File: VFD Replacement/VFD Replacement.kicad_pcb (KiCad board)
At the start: 0 parts

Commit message: Create Display PCB
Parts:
- added D1: LED, LED_SMD:LED_0402_1005Metric, F.Cu at (133.9, 53.1)
- added D10: LED, LED_SMD:LED_0402_1005Metric, F.Cu at (137.2, 57.0)
- added D11: LED, LED_SMD:LED_0402_1005Metric, F.Cu at (138.0, 53.1)
- added D12: LED, LED_SMD:LED_0402_1005Metric, F.Cu at (138.0, 55.7)
- added D13: LED, LED_SMD:LED_0402_1005Metric, F.Cu at (138.0, 58.3)
- added D14: LED, LED_SMD:LED_0402_1005Metric, F.Cu at (138.8, 54.4)
- added D15: LED, LED_SMD:LED_0402_1005Metric, F.Cu at (138.8, 57.0)
- added D16: LED, LED_SMD:LED_0402_1005Metric, F.Cu at (140.0, 58.3)
- added D17: LED, LED_SMD:LED_0402_1005Metric, F.Cu at (141.3, 54.4)
- added D18: LED, LED_SMD:LED_0402_1005Metric, F.Cu at (141.3, 57.0)
- added D19: LED, LED_SMD:LED_0402_1005Metric, F.Cu at (142.2, 53.1)
- added D2: LED, LED_SMD:LED_0402_1005Metric, F.Cu at (133.1, 54.4)
- added D20: LED, LED_SMD:LED_0402_1005Metric, F.Cu at (142.2, 55.7)
- added D21: LED, LED_SMD:LED_0402_1005Metric, F.Cu at (142.2, 58.3)
- added D22: LED, LED_SMD:LED_0402_1005Metric, F.Cu at (143.0, 54.4)
- added D23: LED, LED_SMD:LED_0402_1005Metric, F.Cu at (143.0, 57.0)
- added D24: LED, LED_SMD:LED_0402_1005Metric, F.Cu at (144.2, 58.3)
- added D25: LED, LED_SMD:LED_0402_1005Metric, F.Cu at (145.5, 54.4)
- added D26: LED, LED_SMD:LED_0402_1005Metric, F.Cu at (145.5, 57.0)
- added D27: LED, LED_SMD:LED_0402_1005Metric, F.Cu at (146.3, 53.1)
- added D28: LED, LED_SMD:LED_0402_1005Metric, F.Cu at (146.3, 55.7)
- added D29: LED, LED_SMD:LED_0402_1005Metric, F.Cu at (146.3, 58.3)
- added D3: LED, LED_SMD:LED_0402_1005Metric, F.Cu at (133.1, 57.0)
- added D30: LED, LED_SMD:LED_0402_1005Metric, F.Cu at (147.2, 54.4)
- added D31: LED, LED_SMD:LED_0402_1005Metric, F.Cu at (147.2, 57.0)
- added D32: LED, LED_SMD:LED_0402_1005Metric, F.Cu at (148.3, 58.3)
- added D33: LED, LED_SMD:LED_0402_1005Metric, F.Cu at (149.7, 54.4)
- added D34: LED, LED_SMD:LED_0402_1005Metric, F.Cu at (149.7, 57.0)
- added D35: LED, LED_SMD:LED_0402_1005Metric, F.Cu at (150.5, 53.1)
- added D36: LED, LED_SMD:LED_0402_1005Metric, F.Cu at (150.5, 55.7)
- added D37: LED, LED_SMD:LED_0402_1005Metric, F.Cu at (150.5, 58.3)
- added D38: LED, LED_SMD:LED_0402_1005Metric, F.Cu at (151.3, 54.4)
- added D39: LED, LED_SMD:LED_0402_1005Metric, F.Cu at (151.3, 57.0)
- added D4: LED, LED_SMD:LED_0402_1005Metric, F.Cu at (133.9, 58.3)
- added D40: LED, LED_SMD:LED_0402_1005Metric, F.Cu at (152.5, 58.3)
- added D41: LED, LED_SMD:LED_0402_1005Metric, F.Cu at (153.8, 54.4)
- added D42: LED, LED_SMD:LED_0402_1005Metric, F.Cu at (153.8, 57.0)
- added D43: LED, LED_SMD:LED_0402_1005Metric, F.Cu at (154.6, 53.1)
- added D44: LED, LED_SMD:LED_0402_1005Metric, F.Cu at (154.6, 55.7)
- added D45: LED, LED_SMD:LED_0402_1005Metric, F.Cu at (154.6, 58.3)
- added D46: LED, LED_SMD:LED_0402_1005Metric, F.Cu at (155.4, 54.4)
- added D47: LED, LED_SMD:LED_0402_1005Metric, F.Cu at (155.4, 57.0)
- added D48: LED, LED_SMD:LED_0402_1005Metric, F.Cu at (156.6, 58.3)
- added D49: LED, LED_SMD:LED_0402_1005Metric, F.Cu at (157.9, 54.4)
- added D5: LED, LED_SMD:LED_0402_1005Metric, F.Cu at (133.9, 55.7)
- added D50: LED, LED_SMD:LED_0402_1005Metric, F.Cu at (157.9, 57.0)
- added D51: LED, LED_SMD:LED_0402_1005Metric, F.Cu at (158.8, 53.1)
- added D52: LED, LED_SMD:LED_0402_1005Metric, F.Cu at (158.8, 55.7)
- added D53: LED, LED_SMD:LED_0402_1005Metric, F.Cu at (158.8, 58.3)
- added D54: LED, LED_SMD:LED_0402_1005Metric, F.Cu at (159.6, 54.4)
- added D55: LED, LED_SMD:LED_0402_1005Metric, F.Cu at (159.6, 57.0)
- added D56: LED, LED_SMD:LED_0402_1005Metric, F.Cu at (160.8, 58.3)
- added D57: LED, LED_SMD:LED_0402_1005Metric, F.Cu at (162.1, 54.4)
- added D58: LED, LED_SMD:LED_0402_1005Metric, F.Cu at (162.1, 57.0)
- added D59: LED, LED_SMD:LED_0402_1005Metric, F.Cu at (162.9, 53.1)
- added D6: LED, LED_SMD:LED_0402_1005Metric, F.Cu at (134.7, 54.4)
- added D60: LED, LED_SMD:LED_0402_1005Metric, F.Cu at (162.9, 55.7)
- added D61: LED, LED_SMD:LED_0402_1005Metric, F.Cu at (162.9, 58.3)
- added D62: LED, LED_SMD:LED_0402_1005Metric, F.Cu at (163.8, 54.4)
- added D63: LED, LED_SMD:LED_0402_1005Metric, F.Cu at (163.8, 57.0)
- added D64: LED, LED_SMD:LED_0402_1005Metric, F.Cu at (164.9, 58.3)
- added D65: LED, LED_SMD:LED_0402_1005Metric, F.Cu at (166.2, 54.4)
- added D66: LED, LED_SMD:LED_0402_1005Metric, F.Cu at (166.2, 57.0)
- added D67: LED, LED_SMD:LED_0402_1005Metric, F.Cu at (167.1, 53.1)
- added D68: LED, LED_SMD:LED_0402_1005Metric, F.Cu at (167.1, 55.7)
- added D69: LED, LED_SMD:LED_0402_1005Metric, F.Cu at (167.1, 58.3)
- added D7: LED, LED_SMD:LED_0402_1005Metric, F.Cu at (134.7, 57.0)
- added D70: LED, LED_SMD:LED_0402_1005Metric, F.Cu at (167.9, 54.4)
- added D71: LED, LED_SMD:LED_0402_1005Metric, F.Cu at (167.9, 57.0)
- added D72: LED, LED_SMD:LED_0402_1005Metric, F.Cu at (169.1, 58.3)
- added D73: LED, LED_SMD:LED_0402_1005Metric, F.Cu at (170.4, 54.4)
- added D74: LED, LED_SMD:LED_0402_1005Metric, F.Cu at (170.4, 57.0)
- added D75: LED, LED_SMD:LED_0402_1005Metric, F.Cu at (171.2, 53.1)
- added D76: LED, LED_SMD:LED_0402_1005Metric, F.Cu at (171.2, 55.7)
- added D77: LED, LED_SMD:LED_0402_1005Metric, F.Cu at (171.2, 58.3)
- added D78: LED, LED_SMD:LED_0402_1005Metric, F.Cu at (172.1, 54.4)
- added D79: LED, LED_SMD:LED_0402_1005Metric, F.Cu at (172.1, 57.0)
- added D8: LED, LED_SMD:LED_0402_1005Metric, F.Cu at (135.9, 58.3)
- added D80: LED, LED_SMD:LED_0402_1005Metric, F.Cu at (173.2, 58.3)
- added D81: LED, LED_SMD:LED_0402_1005Metric, F.Cu at (174.6, 54.4)
- added D82: LED, LED_SMD:LED_0402_1005Metric, F.Cu at (174.6, 57.0)
- added D83: LED, LED_SMD:LED_0402_1005Metric, F.Cu at (175.4, 53.1)
- added D84: LED, LED_SMD:LED_0402_1005Metric, F.Cu at (175.4, 55.7)
- added D85: LED, LED_SMD:LED_0402_1005Metric, F.Cu at (175.4, 58.3)
- added D86: LED, LED_SMD:LED_0402_1005Metric, F.Cu at (176.2, 54.4)
- added D87: LED, LED_SMD:LED_0402_1005Metric, F.Cu at (176.2, 57.0)
- added D88: LED, LED_SMD:LED_0402_1005Metric, F.Cu at (177.4, 58.3)
- added D89: LED, LED_SMD:LED_0402_1005Metric, F.Cu at (178.7, 54.4)
- added D9: LED, LED_SMD:LED_0402_1005Metric, F.Cu at (137.2, 54.4)
- added D90: LED, LED_SMD:LED_0402_1005Metric, F.Cu at (178.7, 57.0)
- added D91: LED, LED_SMD:LED_0402_1005Metric, F.Cu at (179.5, 53.1)
- added D92: LED, LED_SMD:LED_0402_1005Metric, F.Cu at (179.5, 55.7)
- added D93: LED, LED_SMD:LED_0402_1005Metric, F.Cu at (179.5, 58.3)
- added D94: LED, LED_SMD:LED_0402_1005Metric, F.Cu at (180.3, 54.4)
- added D95: LED, LED_SMD:LED_0402_1005Metric, F.Cu at (180.3, 57.0)
- added D96: LED, LED_SMD:LED_0402_1005Metric, F.Cu at (181.5, 58.3)
- added J1: Conn_01x05_Pin, footprints:Conn_1x05 2.5mm, F.Cu at (132.0, 44.2)
- added J2: Conn_01x05_Pin, footprints:Conn_1x05 2.5mm, F.Cu at (172.0, 44.2)
- added J3: Conn_01x06_Pin, footprints:Conn_1x06 2.5mm, F.Cu at (132.0, 69.2)
- added J4: Conn_01x06_Pin, footprints:Conn_1x06 2.5mm, F.Cu at (169.5, 69.2)
- added J5: Conn_01x02_Pin, Connector_PinHeader_2.54mm:PinHeader_1x02_P2.54mm_Vertical, F.Cu at (156.5, 68.6)
- added Q1: MMDT2222A, Package_TO_SOT_SMD:SOT-363_SC-70-6, F.Cu at (131.8, 65.0)
- added Q10: MMDT2222A, Package_TO_SOT_SMD:SOT-363_SC-70-6, F.Cu at (147.4, 48.5)
- added Q2: MMDT2222A, Package_TO_SOT_SMD:SOT-363_SC-70-6, F.Cu at (142.2, 65.0)
- added Q3: MMDT2222A, Package_TO_SOT_SMD:SOT-363_SC-70-6, F.Cu at (169.8, 64.8)
- added Q4: MMDT2222A, Package_TO_SOT_SMD:SOT-363_SC-70-6, F.Cu at (181.4, 64.8)
- added Q5: MMDT2222A, Package_TO_SOT_SMD:SOT-363_SC-70-6, F.Cu at (137.1, 65.0)
- added Q6: MMDT2222A, Package_TO_SOT_SMD:SOT-363_SC-70-6, F.Cu at (175.8, 64.8)
- added Q7: MMDT2222A, Package_TO_SOT_SMD:SOT-363_SC-70-6, F.Cu at (167.7, 47.1)
- added Q8: MMDT2222A, Package_TO_SOT_SMD:SOT-363_SC-70-6, F.Cu at (182.7, 47.1)
- added Q9: MMDT2222A, Package_TO_SOT_SMD:SOT-363_SC-70-6, F.Cu at (130.7, 48.4)
- added R1: 10k, Resistor_SMD:R_0603_1608Metric_Pad0.98x0.95mm_HandSolder, F.Cu at (172.0, 46.9)
- added R10: 10k, Resistor_SMD:R_0603_1608Metric_Pad0.98x0.95mm_HandSolder, F.Cu at (174.6, 50.3)
- added R11: 10k, Resistor_SMD:R_0603_1608Metric_Pad0.98x0.95mm_HandSolder, F.Cu at (177.0, 50.3)
- added R12: 10k, Resistor_SMD:R_0603_1608Metric_Pad0.98x0.95mm_HandSolder, F.Cu at (179.4, 50.2)
- added R13: 10k, Resistor_SMD:R_0603_1608Metric_Pad0.98x0.95mm_HandSolder, F.Cu at (134.6, 50.2)
- added R14: 10k, Resistor_SMD:R_0603_1608Metric_Pad0.98x0.95mm_HandSolder, F.Cu at (137.0, 50.2)
- added R15: 10k, Resistor_SMD:R_0603_1608Metric_Pad0.98x0.95mm_HandSolder, F.Cu at (142.0, 50.3)
- added R16: 10k, Resistor_SMD:R_0603_1608Metric_Pad0.98x0.95mm_HandSolder, F.Cu at (139.6, 50.2)
- added R17: 1k, Resistor_SMD:R_0603_1608Metric_Pad0.98x0.95mm_HandSolder, F.Cu at (160.2, 47.4)
- added R18: 1k, Resistor_SMD:R_0603_1608Metric_Pad0.98x0.95mm_HandSolder, F.Cu at (41.1, 39.9)
- added R19: 1k, Resistor_SMD:R_0603_1608Metric_Pad0.98x0.95mm_HandSolder, F.Cu at (45.8, 25.1)
- added R2: 10k, Resistor_SMD:R_0603_1608Metric_Pad0.98x0.95mm_HandSolder, F.Cu at (174.6, 46.9)
- added R20: 1k, Resistor_SMD:R_0603_1608Metric_Pad0.98x0.95mm_HandSolder, F.Cu at (45.8, 28.1)
- added R21: 1k, Resistor_SMD:R_0603_1608Metric_Pad0.98x0.95mm_HandSolder, F.Cu at (45.8, 31.0)
- added R22: 1k, Resistor_SMD:R_0603_1608Metric_Pad0.98x0.95mm_HandSolder, F.Cu at (45.8, 34.0)
- added R23: 1k, Resistor_SMD:R_0603_1608Metric_Pad0.98x0.95mm_HandSolder, F.Cu at (144.9, 48.7)
- added R24: 1k, Resistor_SMD:R_0603_1608Metric_Pad0.98x0.95mm_HandSolder, F.Cu at (149.9, 48.7)
- added R25: 10k, Resistor_SMD:R_0603_1608Metric_Pad0.98x0.95mm_HandSolder, F.Cu at (129.9, 44.9)
- added R3: 10k, Resistor_SMD:R_0603_1608Metric_Pad0.98x0.95mm_HandSolder, F.Cu at (177.0, 46.9)
- added R4: 10k, Resistor_SMD:R_0603_1608Metric_Pad0.98x0.95mm_HandSolder, F.Cu at (179.4, 46.9)
- added R5: 10k, Resistor_SMD:R_0603_1608Metric_Pad0.98x0.95mm_HandSolder, F.Cu at (134.6, 46.9)
- added R6: 10k, Resistor_SMD:R_0603_1608Metric_Pad0.98x0.95mm_HandSolder, F.Cu at (137.0, 46.9)
- added R7: 10k, Resistor_SMD:R_0603_1608Metric_Pad0.98x0.95mm_HandSolder, F.Cu at (142.0, 46.9)
- added R8: 10k, Resistor_SMD:R_0603_1608Metric_Pad0.98x0.95mm_HandSolder, F.Cu at (139.6, 46.9)
- added R9: 10k, Resistor_SMD:R_0603_1608Metric_Pad0.98x0.95mm_HandSolder, F.Cu at (172.0, 50.3)
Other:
- board outline added: 65 x 27.5 mm
- copper layers 0 -> 2
- board text added: "-27V"
- board text added: "-5V"

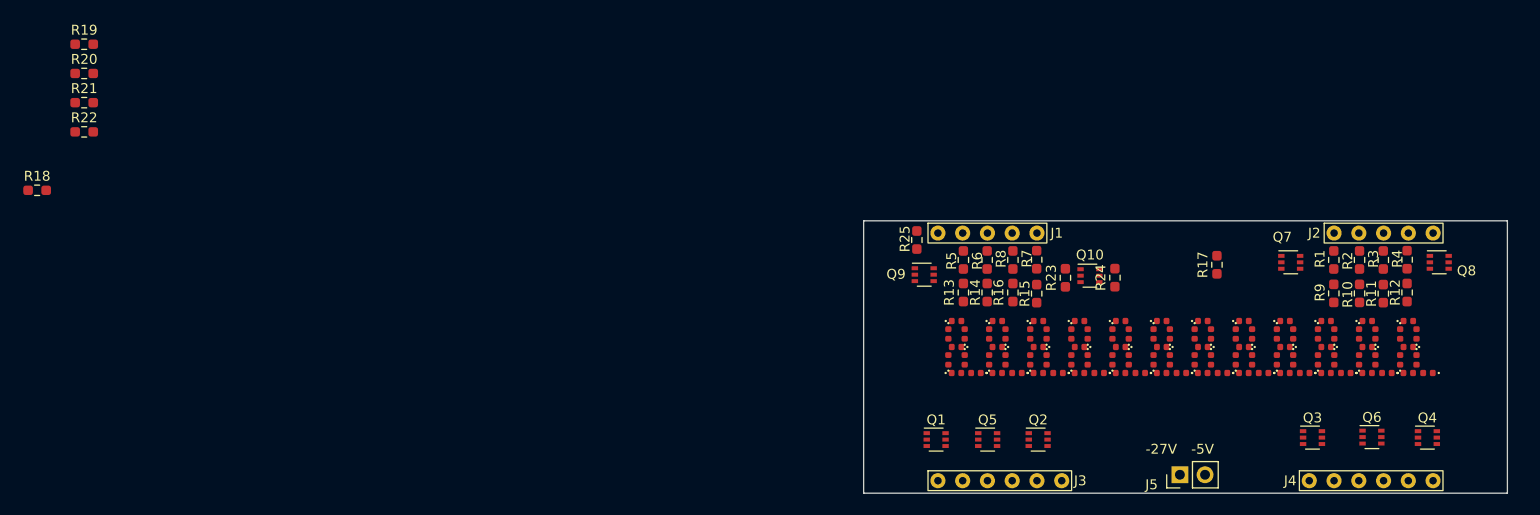
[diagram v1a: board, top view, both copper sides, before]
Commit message: Update VFD Replacement layout
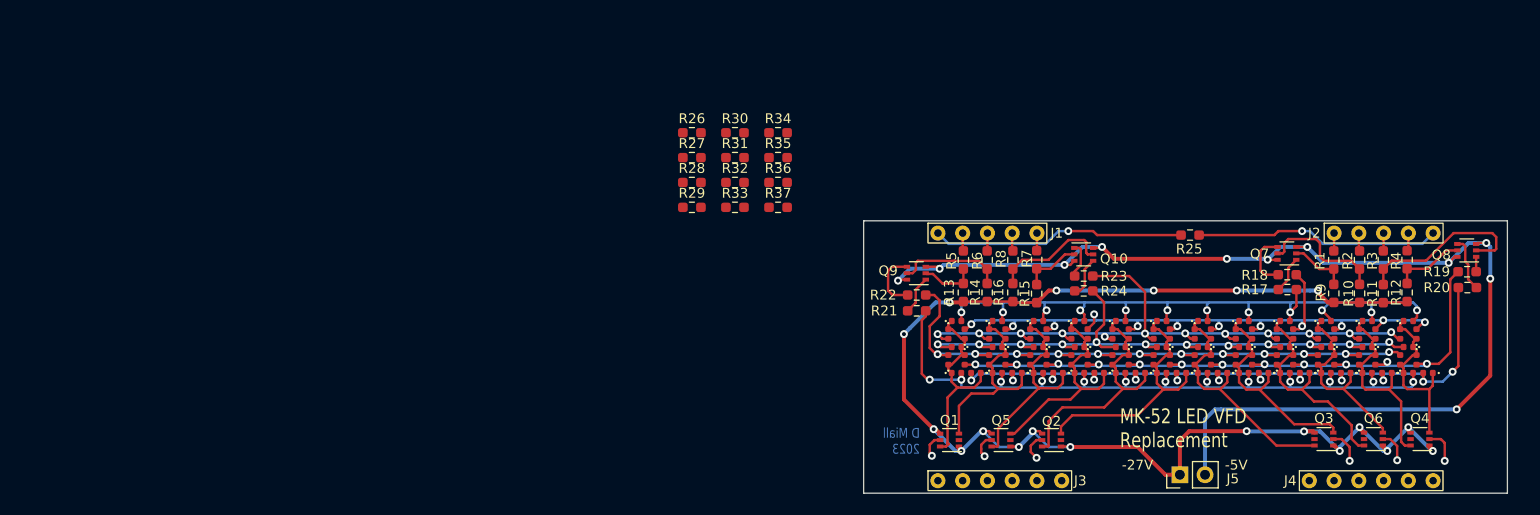
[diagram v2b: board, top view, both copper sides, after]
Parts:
- added R26: 12k, Resistor_SMD:R_0603_1608Metric_Pad0.98x0.95mm_HandSolder, F.Cu at (107.2, 34.1)
- added R27: 12k, Resistor_SMD:R_0603_1608Metric_Pad0.98x0.95mm_HandSolder, F.Cu at (107.2, 36.6)
- added R28: 12k, Resistor_SMD:R_0603_1608Metric_Pad0.98x0.95mm_HandSolder, F.Cu at (107.2, 39.1)
- added R29: 12k, Resistor_SMD:R_0603_1608Metric_Pad0.98x0.95mm_HandSolder, F.Cu at (107.2, 41.6)
- added R30: 12k, Resistor_SMD:R_0603_1608Metric_Pad0.98x0.95mm_HandSolder, F.Cu at (111.5, 34.1)
- added R31: 12k, Resistor_SMD:R_0603_1608Metric_Pad0.98x0.95mm_HandSolder, F.Cu at (111.5, 36.6)
- added R32: 12k, Resistor_SMD:R_0603_1608Metric_Pad0.98x0.95mm_HandSolder, F.Cu at (111.5, 39.1)
- added R33: 12k, Resistor_SMD:R_0603_1608Metric_Pad0.98x0.95mm_HandSolder, F.Cu at (111.5, 41.6)
- added R34: 12k, Resistor_SMD:R_0603_1608Metric_Pad0.98x0.95mm_HandSolder, F.Cu at (115.9, 34.1)
- added R35: 12k, Resistor_SMD:R_0603_1608Metric_Pad0.98x0.95mm_HandSolder, F.Cu at (115.9, 36.6)
- added R36: 12k, Resistor_SMD:R_0603_1608Metric_Pad0.98x0.95mm_HandSolder, F.Cu at (115.9, 39.1)
- added R37: 12k, Resistor_SMD:R_0603_1608Metric_Pad0.98x0.95mm_HandSolder, F.Cu at (115.9, 41.6)
- R1, R2, R3, R4, R5, R6, R7, R8: value 10k -> 1k
- R10, R11, R12, R13, R14, R15, R16, R9: value 10k -> 12k
- R17, R18, R19, R20, R21, R22, R23, R24: value 1k -> 2k4
- moved R19 141.5 mm to (185.5, 48.1)
- moved R20 141.3 mm to (185.5, 49.7)
- moved R18 126.5 mm to (167.3, 48.4), turned to 180 degrees
- moved R21 86.6 mm to (129.9, 52.0), turned to 180 degrees
- moved R22 85.7 mm to (129.9, 50.5), turned to 180 degrees
- moved R25 27.6 mm to (157.5, 44.4), turned to 180 degrees
- moved R17 7.54 mm to (167.3, 49.9), turned to 180 degrees
- moved R24 3.42 mm to (146.8, 50.0), turned to 180 degrees
- moved Q8 3.02 mm to (185.4, 46.0), turned to 180 degrees
- moved Q10 2.24 mm to (146.8, 46.4)
- moved R23 1.86 mm to (146.8, 48.5), turned to 180 degrees
- moved Q1 1.35 mm to (133.2, 65.1), turned to 180 degrees
- moved Q2 1.35 mm to (143.5, 65.1), turned to 180 degrees
- moved Q5 1.35 mm to (138.4, 65.1), turned to 180 degrees
- moved Q3 1.16 mm to (171.0, 65.0), turned to 180 degrees
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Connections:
- Q1 pad 2: /G1 -> Net-(Q1A-B1)
- Q1 pad 5: /G2 -> Net-(Q1B-B2)
- Q2 pad 2: /G5 -> Net-(Q2A-B1)
- Q2 pad 5: /G6 -> Net-(Q2B-B2)
- Q3 pad 2: /G7 -> Net-(Q3A-B1)
- Q3 pad 5: /G8 -> Net-(Q3B-B2)
- Q4 pad 2: /G11 -> Net-(Q4A-B1)
- Q4 pad 3: /G12s -> unconnected-(Q4B-C2-Pad3)
- Q4 pad 5: /G12 -> Net-(Q4B-B2)
- Q4 pad 6: /G11s -> unconnected-(Q4A-C1-Pad6)
- Q5 pad 2: /G3 -> Net-(Q5A-B1)
- Q5 pad 5: /G4 -> Net-(Q5B-B2)
- Q6 pad 2: /G9 -> Net-(Q6A-B1)
- Q6 pad 5: /G10 -> Net-(Q6B-B2)
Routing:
- net -27V: track 0.00 -> 138.7 mm, vias 0 -> 19
- net +22V: track 0.00 -> 122.0 mm, vias 0 -> 11
- net /DPs: track 0.00 -> 74.4 mm, vias 0 -> 13
- net /Ds: track 0.00 -> 74.3 mm, vias 0 -> 13
- net /As: track 0.00 -> 72.8 mm, vias 0 -> 12
- net /Cs: track 0.00 -> 71.7 mm, vias 0 -> 12
- net /Es: track 0.00 -> 70.0 mm, vias 0 -> 12
- net /Bs: track 0.00 -> 69.8 mm, vias 0 -> 12
- net /Fs: track 0.00 -> 69.7 mm, vias 0 -> 12
- net /Gs: track 0.00 -> 69.1 mm, vias 0 -> 12
- net /G6s: track 0.00 -> 26.0 mm
- net /Fil A: track 0.00 -> 25.7 mm, vias 0 -> 1
- net /G7s: track 0.00 -> 25.3 mm
- net /G5s: track 0.00 -> 25.2 mm
- net /Fil B: track 0.00 -> 24.8 mm, vias 0 -> 1
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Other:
- board text added: "D Miall 2023"
- board text added: "JLCJLCJLCJLC"
- board text added: "MK-52 LED VFD Replacement"

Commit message: Complete
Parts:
- removed D1, D10, D11, D12, D13, D14, D15, D16, D17, D18, D19, D2, D20, D21, D22, D23, D24, D25, D26, D27, D28, D29, D3, D30, D31, D32, D33, D34, D35, D36, D37, D38, D39, D4, D40, D41, D42, D43, D44, D45, D46, D47, D48, D49, D5, D50, D51, D52, D53, D54, D55, D56, D57, D58, D59, D6, D60, D61, D62, D63, D64, D65, D66, D67, D68, D69, D7, D70, D71, D72, D73, D74, D75, D76, D77, D78, D79, D8, D80, D81, D82, D83, D84, D85, D86, D87, D88, D89, D9, D90, D91, D92, D93, D94, D95, D96: LED, LED_SMD:LED_0402_1005Metric
- added U1: ~, footprints:display, F.Cu at (148.6, 51.3)
- moved R37 73.4 mm to (184.6, 67.4)
- moved R35 72.2 mm to (181.2, 67.4)
- moved R33 71.2 mm to (177.9, 67.4)
- moved R31 70.2 mm to (174.6, 67.4)
- moved R29 69.1 mm to (171.3, 67.4)
- moved R27 68.2 mm to (168.0, 67.4)
- moved R34 42.7 mm to (142.6, 67.4), turned to 180 degrees
- moved R30 41.3 mm to (135.9, 67.4), turned to 180 degrees
- moved R36 41.3 mm to (145.9, 67.4), turned to 180 degrees
- moved R26 39.9 mm to (129.2, 67.4), turned to 180 degrees
- moved R32 39.6 mm to (139.2, 67.4), turned to 180 degrees
- moved R28 38.0 mm to (132.5, 67.4), turned to 180 degrees
- moved Q3 4.80 mm to (175.7, 63.8), turned to 0 degrees
- moved Q4 4.80 mm to (185.3, 63.8), turned to 0 degrees
- moved Q6 4.80 mm to (180.7, 63.8), turned to 0 degrees
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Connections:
- Q4 pad 3: unconnected-(Q4B-C2-Pad3) -> /G12s
- Q4 pad 6: unconnected-(Q4A-C1-Pad6) -> /G11s
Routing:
- net /Bs: track 69.8 -> 3.66 mm, vias 12 -> 0
- net /As: track 72.8 -> 6.87 mm, vias 12 -> 0
- net /Gs: track 69.1 -> 6.81 mm, vias 12 -> 0
- net /Fs: track 69.7 -> 9.97 mm, vias 12 -> 0
- net /Ds: track 74.3 -> 19.1 mm, vias 13 -> 0
- net /DPs: track 74.4 -> 19.3 mm, vias 13 -> 0
- net /Cs: track 71.7 -> 23.3 mm, vias 12 -> 0
- net /Es: track 70.0 -> 24.5 mm, vias 12 -> 1
- net +22V: track 122.0 -> 103.8 mm, vias 11 -> 8
- net /G5s: track 25.2 -> 14.7 mm
- net -27V: track 138.7 -> 148.1 mm, vias 19 -> 16
- net Net-(Q3B-B2): track 0.00 -> 8.53 mm
- net Net-(Q6B-B2): track 0.00 -> 7.57 mm
- net Net-(Q4B-B2): track 0.00 -> 6.80 mm
- net /G8s: track 22.9 -> 16.2 mm, vias 0 -> 1
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
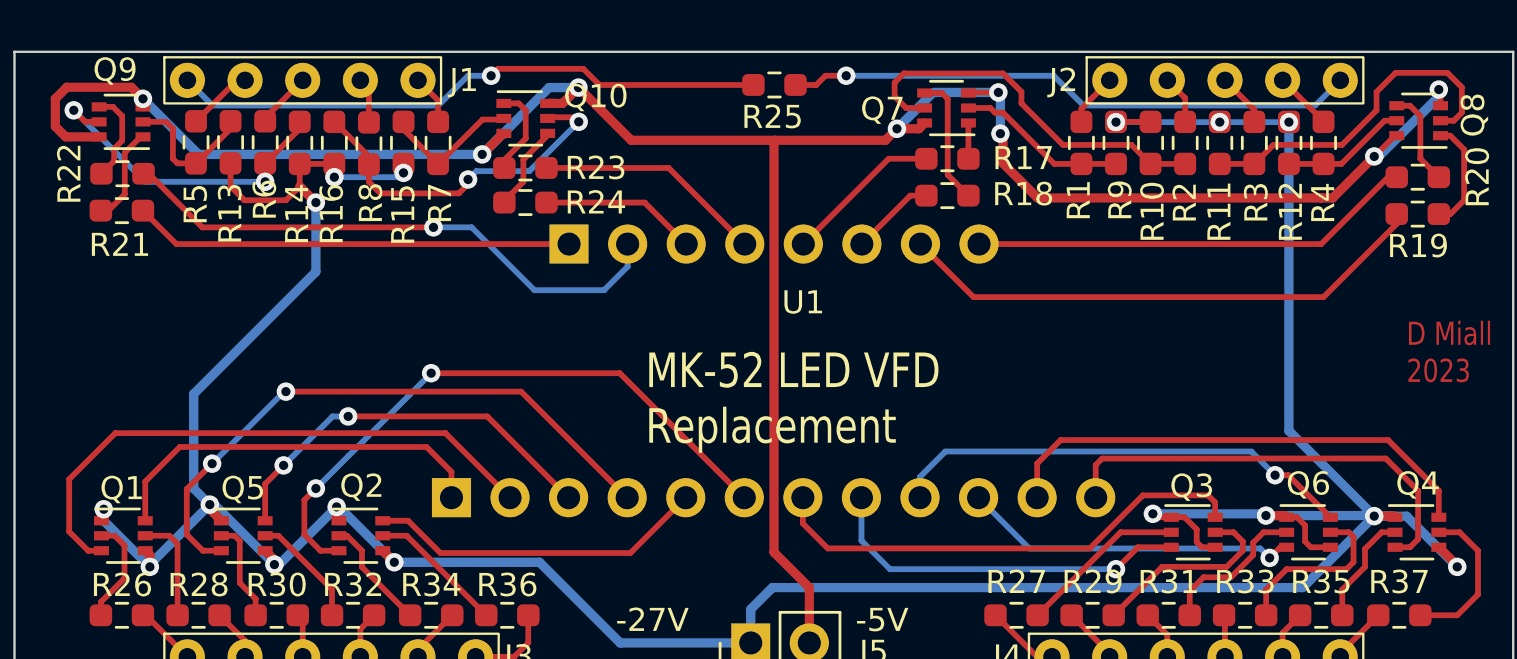
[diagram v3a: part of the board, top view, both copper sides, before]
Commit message: Check 7-seg module and VFD interposer. Create outputs
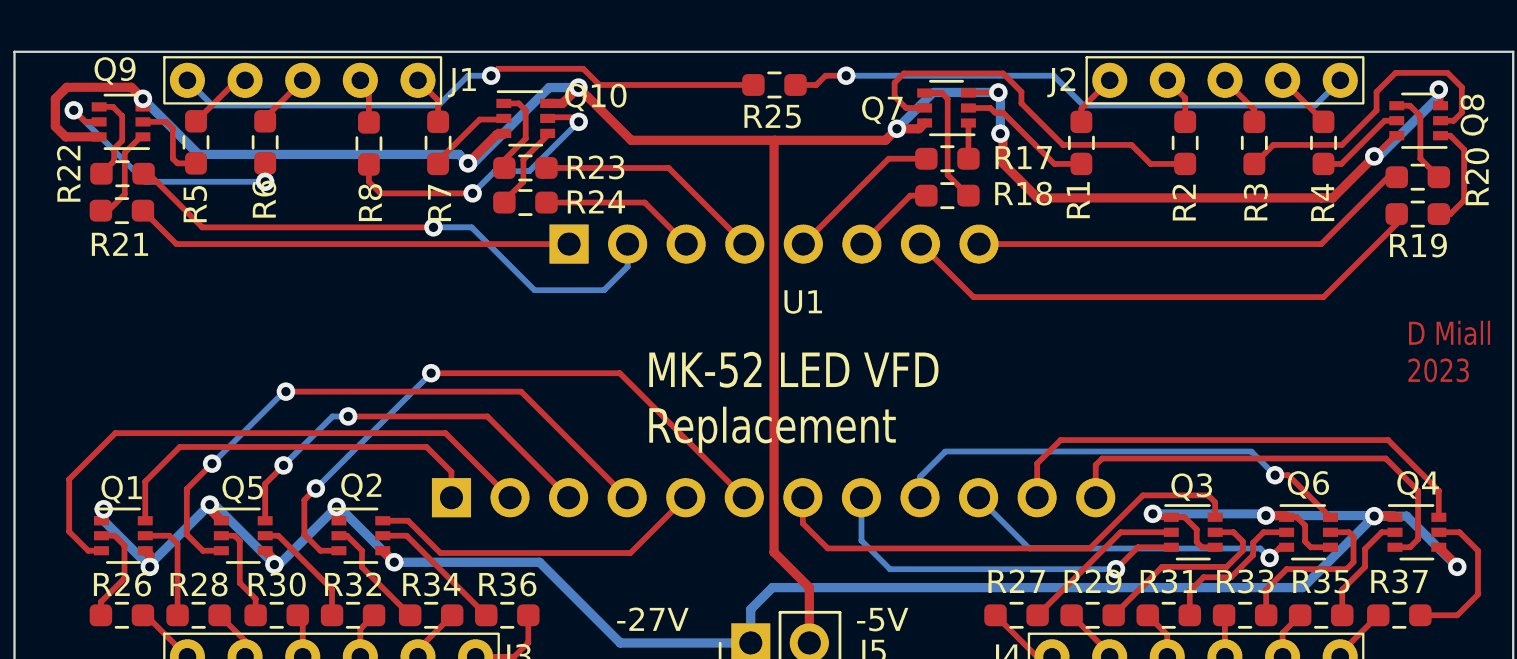
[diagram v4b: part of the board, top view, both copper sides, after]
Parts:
- removed R10, R11, R12, R13, R14, R15, R16, R9: 12k, Resistor_SMD:R_0603_1608Metric_Pad0.98x0.95mm_HandSolder
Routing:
- net -27V: track 148.1 -> 93.3 mm, vias 16 -> 10
- net Net-(Q10B-B2): track 15.4 -> 12.8 mm
- net Net-(Q9A-B1): track 6.25 -> 3.81 mm
- net Net-(Q9B-B2): track 14.1 -> 11.7 mm
- net Net-(Q10A-B1): track 6.09 -> 3.72 mm
- net Net-(Q7A-B1): track 7.40 -> 5.90 mm
- net Net-(Q8B-B2): track 5.45 -> 3.95 mm
- net Net-(Q8A-B1): track 15.0 -> 13.5 mm
- net +22V: track 103.8 -> 104.9 mm

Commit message: Update display base resistor values
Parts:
- R1, R2, R3, R4, R5, R6, R7, R8: value 1k -> 2.4k
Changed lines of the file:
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@@
       (effects (font (size 1 1) (thickness 0.15)))
     )
-    (property "Value" "1k" (at 0 1.43 -90) (layer "F.Fab")
+    (property "Value" "2.4k" (at 0 1.43 -90) (layer "F.Fab")
       (effects (font (size 1 1) (thickness 0.15)))
     )
@@
       (effects (font (size 1 1) (thickness 0.15)))
     )
-    (property "Value" "1k" (at 0.05 0.73 90) (layer "F.Fab")
+    (property "Value" "2.4k" (at 0.05 0.73 90) (layer "F.Fab")
       (effects (font (size 1 1) (thickness 0.15)))
     )
@@
       (effects (font (size 1 1) (thickness 0.15)))
     )
-    (property "Value" "1k" (at -0.0125 1.43 90) (layer "F.Fab")
+    (property "Value" "2.4k" (at -0.0125 1.43 90) (layer "F.Fab")
       (effects (font (size 1 1) (thickness 0.15)))
     )
@@
       (effects (font (size 1 1) (thickness 0.15)))
     )
-    (property "Value" "1k" (at 0 1.43 90) (layer "F.Fab")
+    (property "Value" "2.4k" (at 0 1.43 90) (layer "F.Fab")
       (effects (font (size 1 1) (thickness 0.15)))
     )
@@
       (effects (font (size 1 1) (thickness 0.15)))
     )
-    (property "Value" "1k" (at 0 1.43 90) (layer "F.Fab")
+    (property "Value" "2.4k" (at 0 1.43 90) (layer "F.Fab")
       (effects (font (size 1 1) (thickness 0.15)))
     )
@@
       (effects (font (size 1 1) (thickness 0.15)))
     )
-    (property "Value" "1k" (at 0 1.43 90) (layer "F.Fab")
+    (property "Value" "2.4k" (at 0 1.43 90) (layer "F.Fab")
       (effects (font (size 1 1) (thickness 0.15)))
     )
@@
       (effects (font (size 1 1) (thickness 0.15)))
     )
-    (property "Value" "1k" (at 0 1.43 90) (layer "F.Fab")
+    (property "Value" "2.4k" (at 0 1.43 90) (layer "F.Fab")
       (effects (font (size 1 1) (thickness 0.15)))
     )
@@
       (effects (font (size 1 1) (thickness 0.15)))
     )
-    (property "Value" "1k" (at 0 1.43 90) (layer "F.Fab")
-      (effects (font (size 1 1) (thickness 0.15)))
-    )
+    (property "Value" "2.4k" (at 0 1.43 90) (layer "F.Fab")
+      (effects (font (size 1 1) (thickness 0.15)))
+    )
